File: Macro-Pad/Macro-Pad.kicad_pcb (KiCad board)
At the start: 2 copper layers, 42 x 80.5 mm, 14 parts, among them J1 USB_C_Receptacle_USB2.0_14P, U1 ESP32-S3-WROOM-1, U2 TPS62162DSG

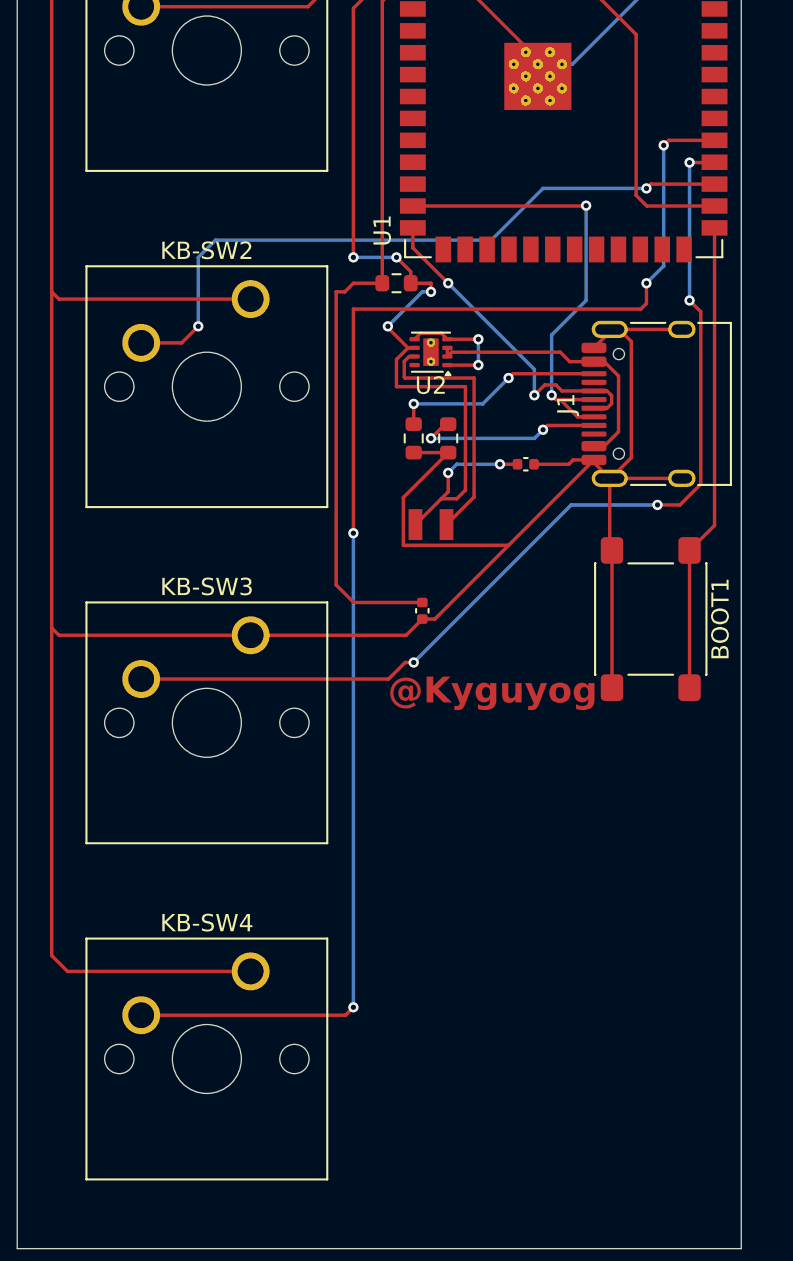
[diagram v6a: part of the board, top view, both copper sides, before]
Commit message: Added silkscreen text
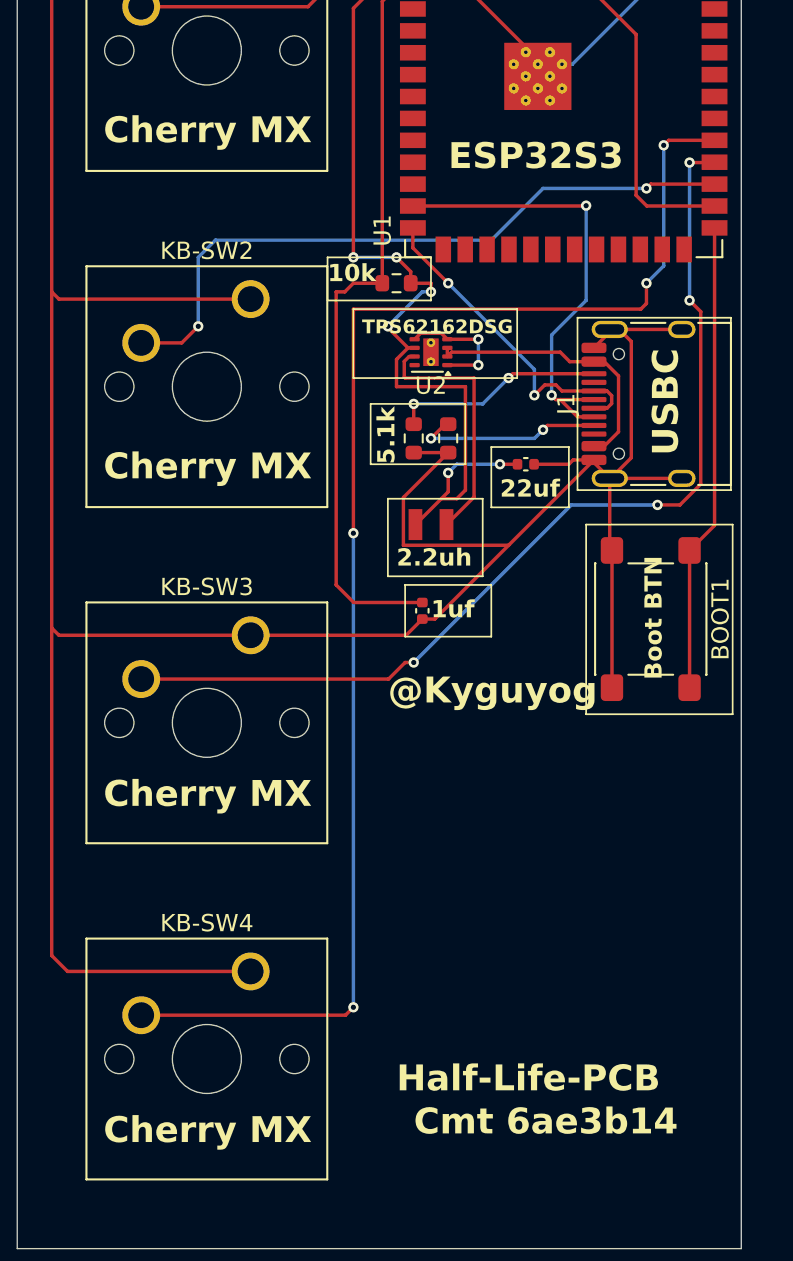
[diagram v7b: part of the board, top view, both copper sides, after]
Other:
- board text added: "10k"
- board text added: "1uf"
- board text added: "2.2uh"
- board text added: "22uf"
- board text added: "5.1k"
- board text added: "Boot BTN"
- board text added: "Cherry MX"
- board text added: "Cmt 6ae3b14"
- board text added: "ESP32S3"
- board text added: "Half-Life-PCB"
- board text added: "TPS62162DSG"
- board text added: "USBC"

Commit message: re-format everything to save and optimize space
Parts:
- removed C2: 22uF, PCM_SparkFun-Capacitor:C_0402_1005Metric
- removed J1: USB_C_Receptacle_USB2.0_14P, Connector_USB:USB_C_Receptacle_HRO_TYPE-C-31-M-12
- removed L1: 2.2uH, PCM_SparkFun-Coil:0806
- removed U2: TPS62162DSG, Package_SON:Texas_DSG0008A_WSON-8-1EP_2x2mm_P0.5mm_EP0.9x1.6mm_ThermalVias
- added BUCK1: AMS1117-3.3, Package_TO_SOT_SMD:SOT-223-3_TabPin2, F.Cu at (124.2, 103.8)
- added IN_CAP1: 10uF, Capacitor_SMD:C_0805_2012Metric_Pad1.18x1.45mm_HandSolder, F.Cu at (121.5, 113.5)
- added OUT_CAP1: 22uF, Capacitor_SMD:C_0805_2012Metric_Pad1.18x1.45mm_HandSolder, F.Cu at (123.0, 96.5)
- added USBC1: USB_C_Receptacle_USB2.0_14P, Connector_USB:USB_C_Receptacle_HRO_TYPE-C-31-M-12, F.Cu at (130.2, 120.5)
- BOOT1: footprint Button_Switch_SMD:SW_SPST_PTS645Sx43SMTR92 -> Button_Switch_SMD:SW_Push_SPST_NO_Alps_SKRK
- C1: footprint PCM_SparkFun-Capacitor:C_0402_1005Metric -> Capacitor_SMD:C_0805_2012Metric_Pad1.18x1.45mm_HandSolder
- R1, R2, R3: footprint PCM_SparkFun-Resistor:R_0603_1608Metric -> Resistor_SMD:R_0805_2012Metric_Pad1.20x1.40mm_HandSolder
- moved R3 97.2 mm to (125.5, 73.0)
- moved R2 96.6 mm to (123.0, 88.5), turned to 180 degrees
- moved R1 95.9 mm to (123.0, 91.0), turned to 180 degrees
- moved C1 90.9 mm to (125.5, 75.0), turned to 0 degrees
- moved KB-SW1 90.6 mm to (112.0, 49.0)
- moved KB-SW2 90.6 mm to (112.0, 68.5)
- moved KB-SW3 90.6 mm to (112.0, 88.0)
- moved KB-SW4 90.6 mm to (112.0, 107.5)
- moved U1 90.2 mm to (129.5, 53.6)
- moved BOOT1 86.4 mm to (134.5, 74.0), turned to 180 degrees
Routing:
- net Net-(U1-USB_D+): track 19.2 -> 65.9 mm
- net Net-(U1-USB_D-): track 26.8 -> 63.6 mm
- net Net-(BUCK1-VI): track 0.00 -> 23.2 mm
- net Net-(USBC1-CC2): track 12.4 -> 31.5 mm, vias 2 -> 0
- net Net-(U1-IO0): track 27.3 -> 9.78 mm
- net Net-(USBC1-CC1): track 11.1 -> 27.8 mm, vias 2 -> 0
- net Net-(U1-EN): track 43.8 -> 27.3 mm, vias 0 -> 2
- net Net-(BUCK1-VO): track 52.5 -> 69.0 mm, vias 6 -> 4
- net Net-(U2-EN): track 16.1 -> 0.00 mm
- net Net-(U2-SW): track 14.9 -> 0.00 mm
- net Net-(U1-IO36): track 39.4 -> 50.6 mm, vias 2 -> 0
- net Net-(U2-AGND): track 7.29 -> 0.00 mm, vias 2 -> 0
- net (no net): track 0.00 -> 5.13 mm
- net Net-(BUCK1-GND): track 234.0 -> 238.9 mm, vias 1 -> 0
- net Net-(U1-IO37): track 57.5 -> 61.0 mm, vias 4 -> 2
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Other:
- board size 42 x 80.5 mm -> 42 x 79.5 mm
- board text removed: "1uf"
- board text removed: "2.2uh"
- board text removed: "22uf"
- board text removed: "5.1k"
- board text removed: "@Kyguyog"
- board text removed: "Boot BTN"
- board text removed: "Cmt 6ae3b14"
- board text removed: "ESP32S3"
- board text removed: "Half-Life-PCB"
- board text removed: "TPS62162DSG"
- board text removed: "USBC"
